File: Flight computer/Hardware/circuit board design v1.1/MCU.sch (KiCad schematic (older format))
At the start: 30 parts, among them J1 Conn_01x05, U11 W25Q64JVSSIM, U7 ATSAMD21J18A-AU, Y3 16MHz

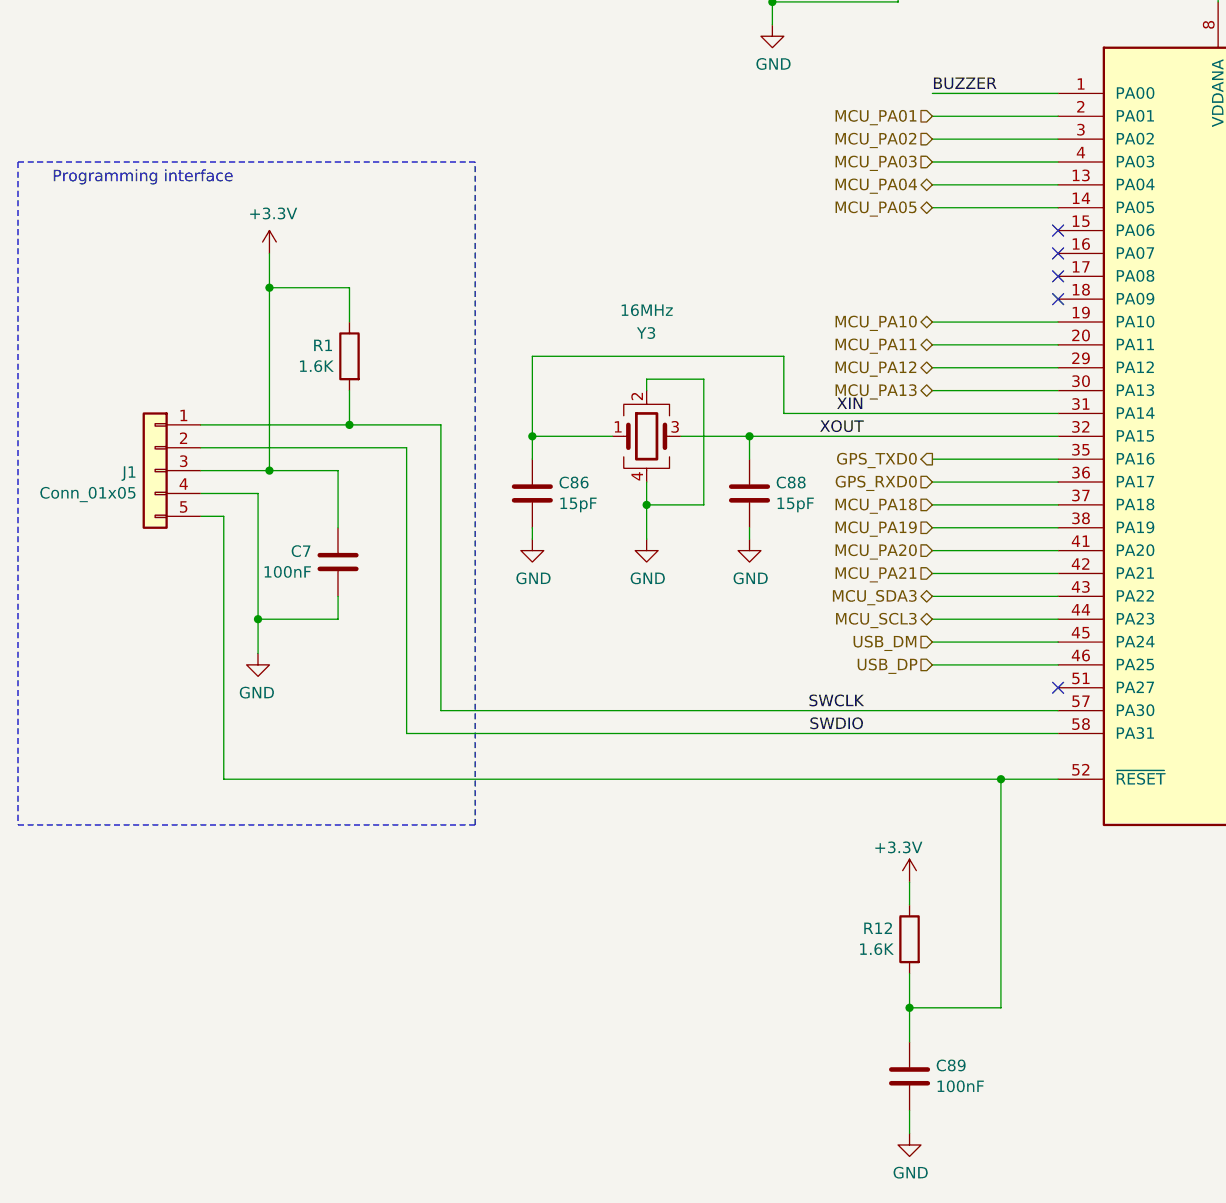
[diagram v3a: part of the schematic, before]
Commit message: added in grove connector for break out pins. Made a new software framework for SAMD
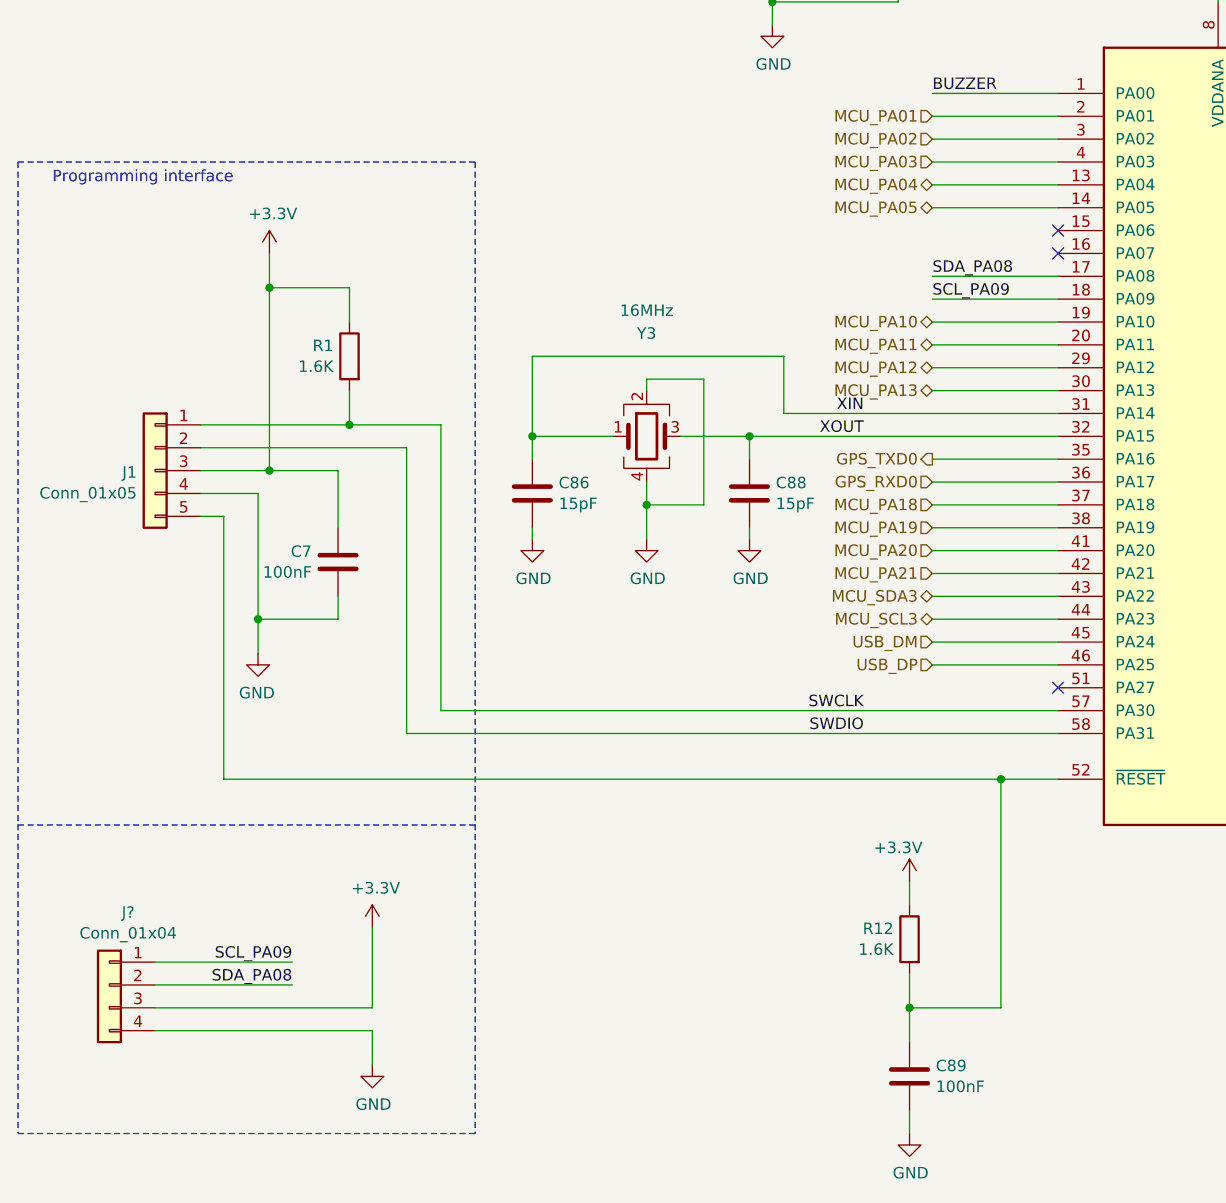
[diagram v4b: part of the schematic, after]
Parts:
- added J?: Conn_01x04, Connector:NS-Tech_Grove_1x04_P2mm_Vertical, symbol Connector_Generic:Conn_01x04
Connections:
- net +3V3: now also J?.3 (Pin_3)
- net GND: now also J?.4 (Pin_4)
- net SDA_PA08: now reaches U7.17 (PA08)
- net SDA_PA08: now also J?.2 (Pin_2)
- net SCL_PA09: now reaches U7.18 (PA09)
- net SCL_PA09: now also J?.1 (Pin_1)
- no-connect marks 14 -> 12
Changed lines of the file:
@@
 	1450 4750 1450 5900
 Connection ~ 4850 5900
-Wire Notes Line
-	2550 6100 2550 3200
-Wire Notes Line
-	550  3200 550  6100
 Wire Wire Line
 	3900 4050 2800 4050
@@
 	1    0    0    -1
 $EndComp
+NoConn ~ 5100 3600
+NoConn ~ 5100 3500
+Text HLabel 4550 4700 0    50   Input ~ 0
+MCU_PA18
+Wire Wire Line
+	4550 4700 5100 4700
+Text HLabel 4550 4800 0    50   Input ~ 0
+MCU_PA19
+Wire Wire Line
+	4550 4800 5100 4800
+$Comp
+L Connector_Generic:Conn_01x04 J?
+U 1 1 5D96BBFC
+P 950 6800
+F 0 "J?" H 868 7117 50  0000 C CNN
+F 1 "Conn_01x04" H 868 7026 50  0000 C CNN
+F 2 "Connector:NS-Tech_Grove_1x04_P2mm_Vertical" H 950 6800 50  0001 C CNN
+F 3 "~" H 950 6800 50  0001 C CNN
+	1    950  6800
+	-1   0    0    -1
+$EndComp
 $Comp
 L flight-computer:ATSAMD21J18A-AU U7
@@
 	1    0    0    -1
 $EndComp
-NoConn ~ 5100 3800
-NoConn ~ 5100 3700
-NoConn ~ 5100 3600
-NoConn ~ 5100 3500
-Text HLabel 4550 4700 0    50   Input ~ 0
-MCU_PA18
-Wire Wire Line
-	4550 4700 5100 4700
-Text HLabel 4550 4800 0    50   Input ~ 0
-MCU_PA19
-Wire Wire Line
-	4550 4800 5100 4800
+Wire Wire Line
+	1150 6800 1750 6800
+Wire Notes Line
+	550  7450 2550 7450
+Wire Notes Line
+	2550 3200 2550 7450
+Wire Notes Line
+	550  3200 550  7450
+Text Label 4550 3700 0    50   ~ 0
+SDA_PA08
+Text Label 4550 3800 0    50   ~ 0
+SCL_PA09
+Wire Wire Line
+	4550 3700 5100 3700
+Wire Wire Line
+	4550 3800 5100 3800
+Text Label 1750 6800 2    50   ~ 0
+SDA_PA08
+Text Label 1750 6700 2    50   ~ 0
+SCL_PA09
+Wire Wire Line
+	1150 6700 1750 6700
+Wire Wire Line
+	2100 6900 2100 6550
+Wire Wire Line
+	1150 6900 2100 6900
+$Comp
+L power:+3.3V #PWR?
+U 1 1 5DA417EA
+P 2100 6550
+F 0 "#PWR?" H 2100 6400 50  0001 C CNN
+F 1 "+3.3V" H 2115 6723 50  0000 C CNN
+F 2 "" H 2100 6550 50  0001 C CNN
+F 3 "" H 2100 6550 50  0001 C CNN
+	1    2100 6550
+	1    0    0    -1
+$EndComp
+Wire Wire Line
+	1150 7000 2100 7000
+Wire Wire Line
+	2100 7000 2100 7150
+$Comp
+L power:GND #PWR?
+U 1 1 5DA4D92B
+P 2100 7150
+F 0 "#PWR?" H 2100 6900 50  0001 C CNN
+F 1 "GND" H 2105 6977 50  0000 C CNN
+F 2 "" H 2100 7150 50  0001 C CNN
+F 3 "" H 2100 7150 50  0001 C CNN
+	1    2100 7150
+	1    0    0    -1
+$EndComp
 $EndSCHEMATC
